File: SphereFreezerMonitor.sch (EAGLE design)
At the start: 8 parts

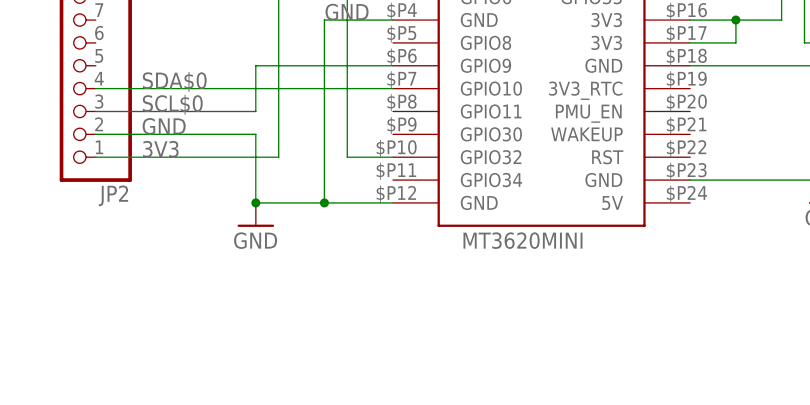
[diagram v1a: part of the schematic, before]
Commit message: Add terminal block for reed switch
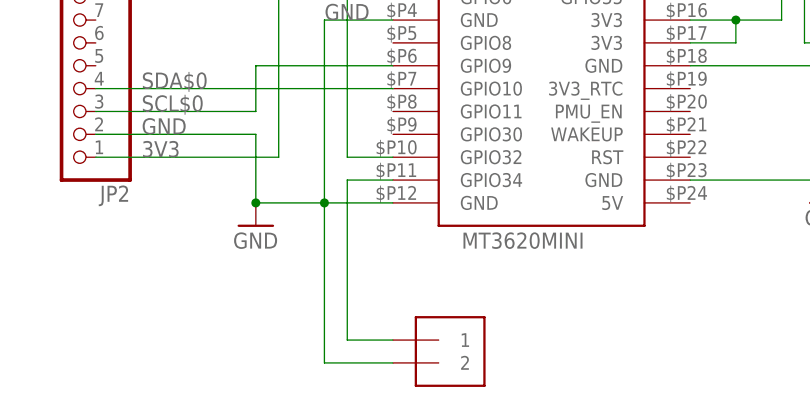
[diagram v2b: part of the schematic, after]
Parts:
- added J1: 1X2-3.5MM, adafruit:1X2-3.5MM
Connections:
- new net N$1: J1.1, U$1.GPIO34
- net GND: now also J1.2
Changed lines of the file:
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@@
 <part name="GND4" library="SparkFun-PowerSymbols" library_urn="urn:adsk.eagle:library:530" deviceset="GND" device=""/>
 <part name="FRAME1" library="frames" library_urn="urn:adsk.eagle:library:229" deviceset="FRAME_A_L" device=""/>
+<part name="J1" library="adafruit" deviceset="1X2" device="-3.5MM"/>
 </parts>
 <sheets>
@@
 <attribute name="DRAWING_NAME" x="116.84" y="-41.91" size="2.54" layer="94"/>
 </instance>
+<instance part="J1" gate="G$1" x="48.26" y="7.62" smashed="yes"/>
 </instances>
 <busses>
@@
 <junction x="35.56" y="25.4"/>
 <label x="15.24" y="33.02" size="1.778" layer="95"/>
+<pinref part="J1" gate="G$1" pin="2"/>
+<wire x1="43.18" y1="7.62" x2="35.56" y2="7.62" width="0.1524" layer="91"/>
+<wire x1="35.56" y1="7.62" x2="35.56" y2="25.4" width="0.1524" layer="91"/>
 </segment>
 <segment>
@@
 </segment>
 </net>
+<net name="N$1" class="0">
+<segment>
+<pinref part="U$1" gate="G$1" pin="GPIO34"/>
+<wire x1="43.18" y1="27.94" x2="38.1" y2="27.94" width="0.1524" layer="91"/>
+<pinref part="J1" gate="G$1" pin="1"/>
+<wire x1="38.1" y1="27.94" x2="38.1" y2="10.16" width="0.1524" layer="91"/>
+<wire x1="38.1" y1="10.16" x2="43.18" y2="10.16" width="0.1524" layer="91"/>
+</segment>
+</net>

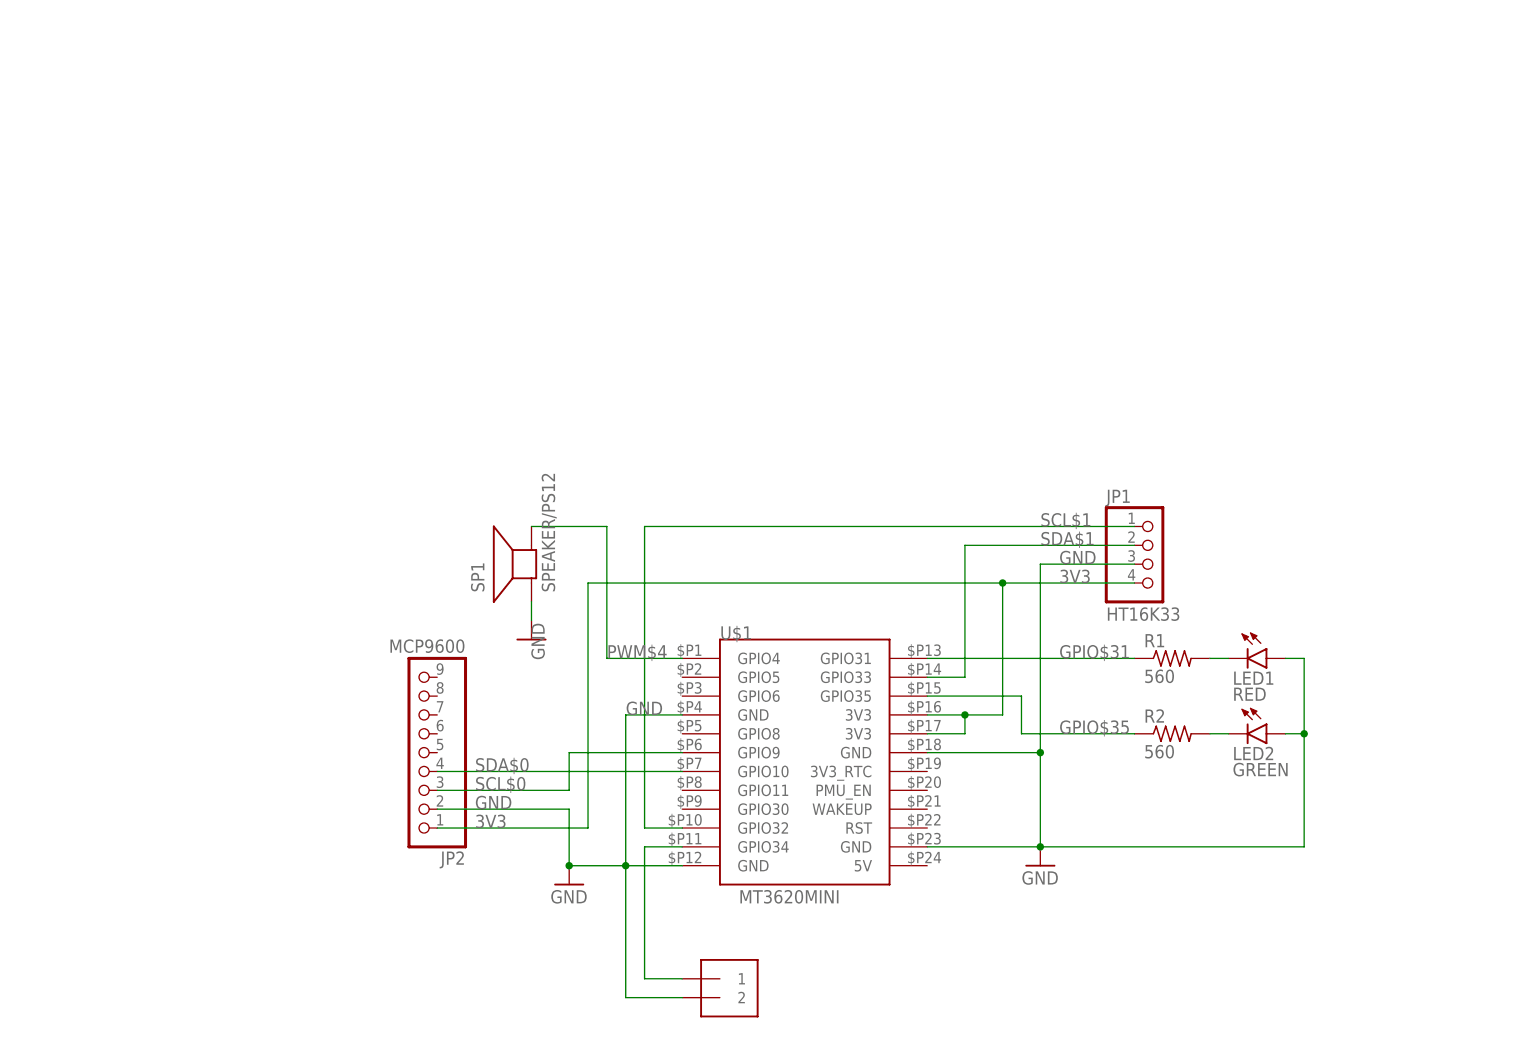
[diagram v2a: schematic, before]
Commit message: Update schematic for pinmux conflicts and add pull-up and bypass on mag-swtich
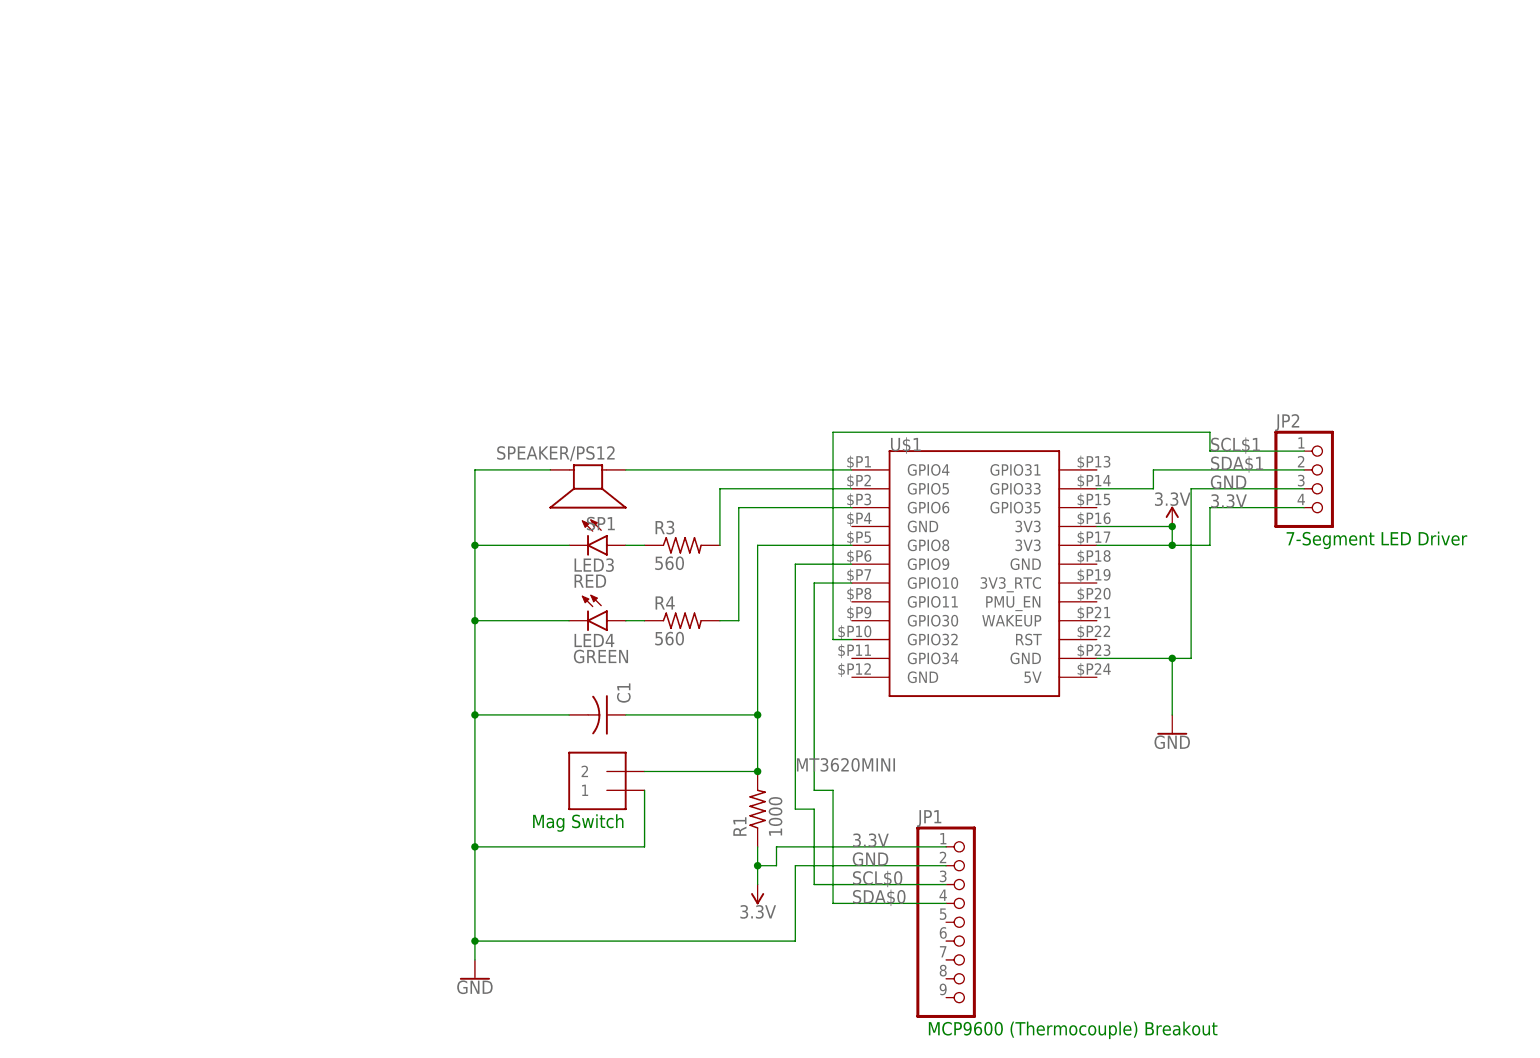
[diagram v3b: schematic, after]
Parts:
- removed LED1: RED, led:LED10MM
- removed LED2: GREEN, led:LED10MM
- removed R2: 560, adafruit:R-US_0207/9
- added C1: (no value), adafruit:C-US025-025X050
- added LED3: RED, led:LED10MM
- added LED4: GREEN, led:LED10MM
- added R3, R4: 560, adafruit:R-US_0207/9
- JP1: value HT16K33 -> (none); device pinhead:PINHD-1X4 -> adafruit:PINHD-1X9
- JP2: value MCP9600 -> (none); device pinhead:PINHD-1X9 -> pinhead:PINHD-1X4
- R1: value 560 -> 1000
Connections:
- removed net 3V3: JP1.4, JP2.1, U$1.3V3@1, U$1.3V3@2
- removed net GPIO$31: R1.1, U$1.GPIO31
- removed net GPIO$35: R2.1, U$1.GPIO35
- removed net PWM$4: SP1.-, U$1.GPIO4
- new net 3.3V: JP1.1, JP2.4, R1.1, U$1.3V3@1, U$1.3V3@2
- new net N$2: R3.2, U$1.GPIO5
- new net N$3: R4.2, U$1.GPIO6
- new net N$4: C1.1, J1.2, R1.2, U$1.GPIO8
- net GND: now also C1.2, J1.1, JP1.2, JP2.3, LED3.C, LED4.C, SP1.-; no longer J1.2, JP1.3, JP2.2, LED1.A, LED2.A, SP1.+, U$1.GND, U$1.GND@2, U$1.GND@3
- net N$1: now also SP1.+, U$1.GPIO4; no longer J1.1, U$1.GPIO34
- net N$5: now also LED3.A, R3.1; no longer LED1.C, R1.2
- net N$6: now also LED4.A, R4.1; no longer LED2.C, R2.2
- net SCL$0: now also JP1.3; no longer JP2.3
- net SCL$1: now also JP2.1; no longer JP1.1
- net SDA$0: now also JP1.4; no longer JP2.4
- net SDA$1: now also JP2.2; no longer JP1.2
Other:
- note added: "7-Segment LED Driver"
- note added: "MCP9600 (Thermocouple) Breakout"
- note added: "Mag Switch"
- moved on the sheet: R1, SP1, U$1

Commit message: Update to use 1 I2C and use PWM for buzzer
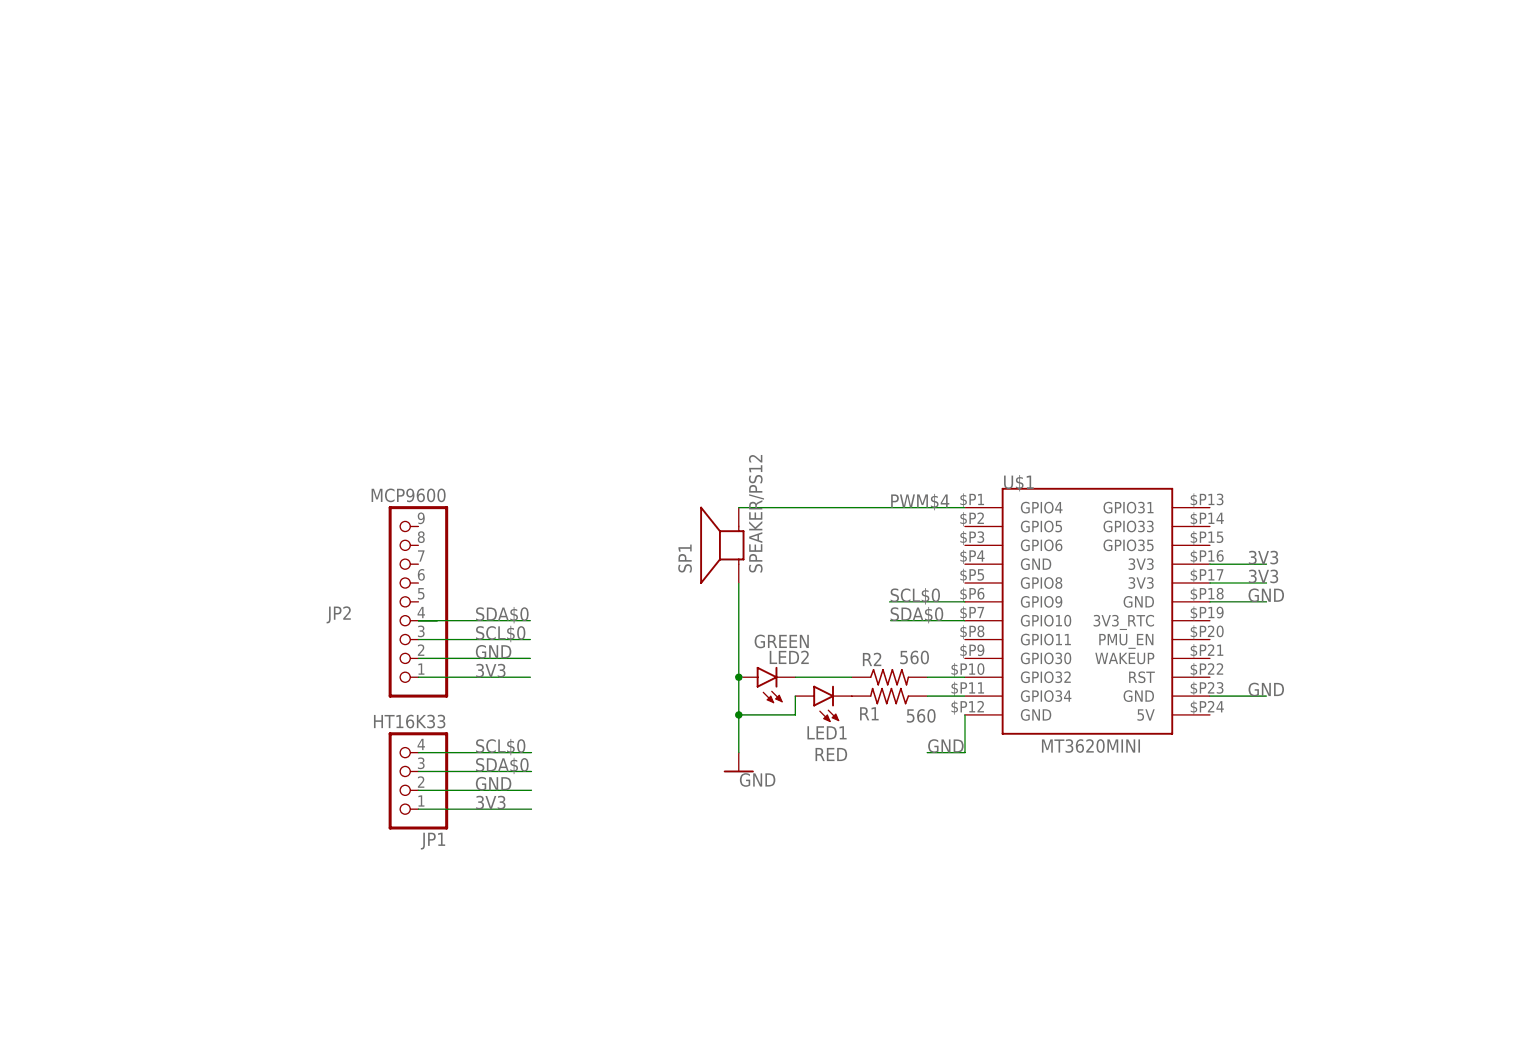
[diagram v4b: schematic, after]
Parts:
- removed C1: (no value), adafruit:C-US025-025X050
- removed J1: 1X2-3.5MM, adafruit:1X2-3.5MM
- removed LED3: RED, led:LED10MM
- removed LED4: GREEN, led:LED10MM
- removed R3, R4: 560, adafruit:R-US_0207/9
- added LED1: RED, led:LED10MM
- added LED2: GREEN, led:LED10MM
- added R2: 560, adafruit:R-US_0207/9
- JP1: value (none) -> HT16K33; device adafruit:PINHD-1X9 -> pinhead:PINHD-1X4
- JP2: value (none) -> MCP9600; device pinhead:PINHD-1X4 -> pinhead:PINHD-1X9
- R1: value 1000 -> 560
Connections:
- removed net 3.3V: JP1.1, JP2.4, R1.1, U$1.3V3@1, U$1.3V3@2
- removed net N$4: C1.1, J1.2, R1.2, U$1.GPIO8
- removed net N$6: LED4.A, R4.1
- removed net SCL$1: JP2.1, U$1.GPIO32
- removed net SDA$1: JP2.2, U$1.GPIO33
- new net 3V3: JP1.1, JP2.1, U$1.3V3@1, U$1.3V3@2
- new net PWM$4: SP1.-, U$1.GPIO4
- net GND: now also JP2.2, LED1.A, LED2.A, SP1.+, U$1.GND@2, U$1.GND@3; no longer C1.2, J1.1, JP2.3, LED3.C, LED4.C, SP1.-
- net N$1: now also R1.1, U$1.GPIO34; no longer SP1.+, U$1.GPIO4
- net N$2: now also LED2.C, R2.1; no longer R3.2, U$1.GPIO5
- net N$3: now also R2.2, U$1.GPIO32; no longer R4.2, U$1.GPIO6
- net N$5: now also LED1.C, R1.2; no longer LED3.A, R3.1
- net SCL$0: now also JP1.4, JP2.3; no longer JP1.3
- net SDA$0: now also JP1.3, JP2.4; no longer JP1.4
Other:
- note removed: "7-Segment LED Driver"
- note removed: "MCP9600 (Thermocouple) Breakout"
- note removed: "Mag Switch"
- moved on the sheet: R1, SP1, U$1

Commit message: Update schematic for debounce & mag-switch
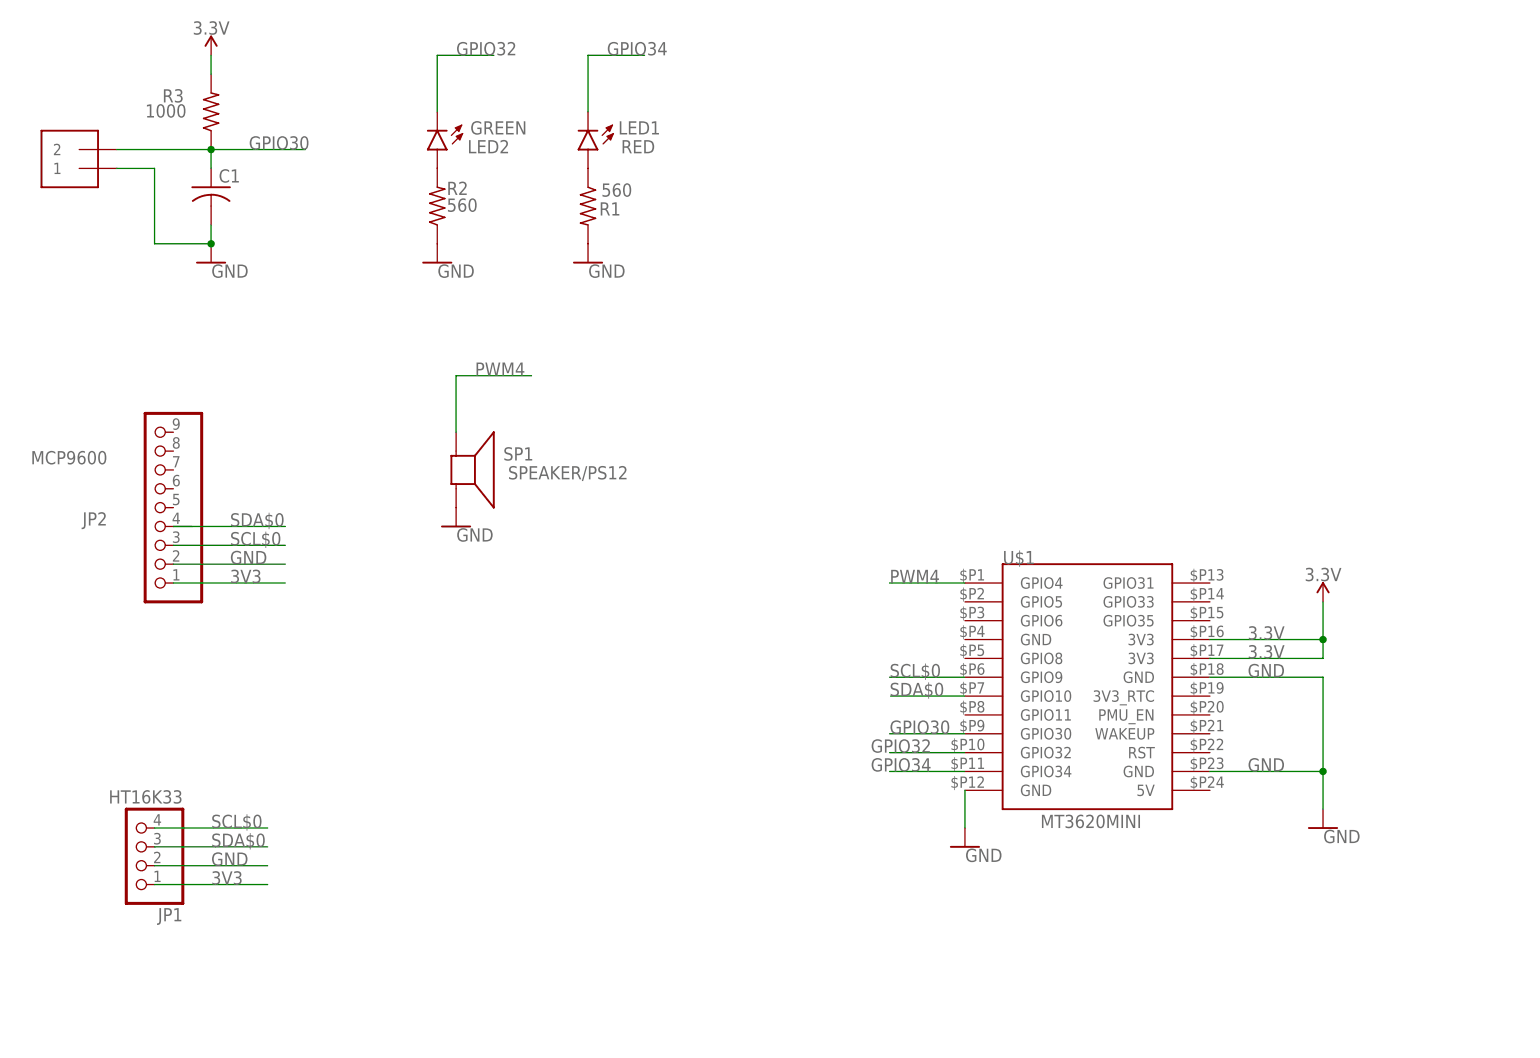
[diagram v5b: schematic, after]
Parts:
- added C1: (no value), adafruit:C-US025-025X050
- added J1: 1X2-3.5MM, adafruit:1X2-3.5MM
- added R3: 1000, adafruit:R-US_0207/9
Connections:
- removed net N$3: R2.2, U$1.GPIO32
- removed net N$5: LED1.C, R1.2
- removed net PWM$4: SP1.-, U$1.GPIO4
- new net 3.3V: R3.2, U$1.3V3@1, U$1.3V3@2
- new net GPIO30: C1.1, J1.2, R3.1, U$1.GPIO30
- new net GPIO32: LED2.C, U$1.GPIO32
- new net GPIO34: LED1.C, U$1.GPIO34
- new net PWM4: SP1.+, U$1.GPIO4
- net 3V3: no longer U$1.3V3@1, U$1.3V3@2
- net GND: now also C1.2, J1.1, R1.2, R2.1, SP1.-; no longer LED1.A, LED2.A, SP1.+
- net N$1: now also LED1.A; no longer U$1.GPIO34
- net N$2: now also LED2.A, R2.2; no longer LED2.C, R2.1
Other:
- moved on the sheet: JP1, JP2, LED1, LED2, R1, R2, SP1, U$1
